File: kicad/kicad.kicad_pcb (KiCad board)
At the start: 2 copper layers, 106 parts, among them K0 !,,,,,,1, K1 ",,,,,,2, K10 *,,,,,,:, K11 =,,,,,,-, K12 Break, K13 Up, K14 Q, K15 W, K16 E, K17 R, K18 T, K19 Y, K2 #,,,,,,3, K20 U, K21 I, K22 O, K23 P, K24 @, K25 Left, K26 Right, K27 Down, K28 A, K29 S, K3 $,,,,,,4, K30 D, K31 F, K32 G, K33 H, K34 J, K35 K, K36 L, K37 +,,,,,,;, K38 ENTER, K39 CLEAR, K4 %,,,,,,5, K40 SHIFT, K41 Z, K42 X, K43 C, K44 V, K45 B, K46 N, K47 M, K48 <,,,,,,,, K49 >,,,,,,., K5 &,,,,,,6, K50 ?,,,,,,/, K51 SHIFT, K52 Blank, K6 ',,,,,,7, K7 (,,,,,,8, K8 ),,,,,,9, K9 0

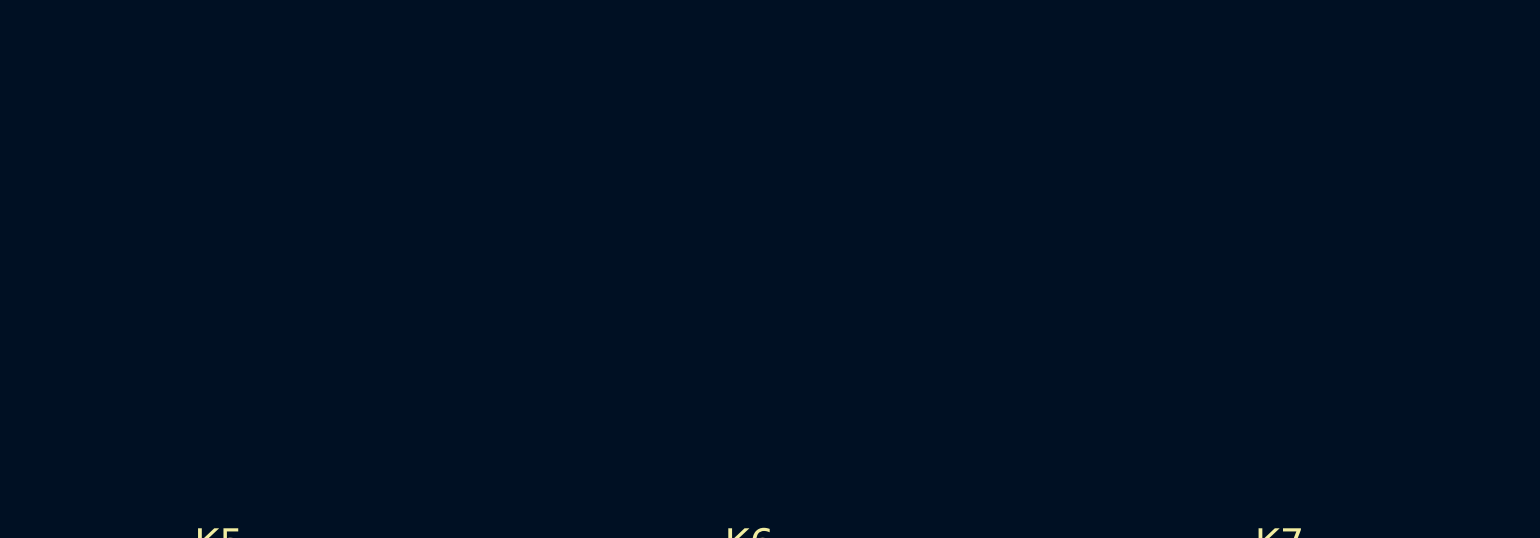
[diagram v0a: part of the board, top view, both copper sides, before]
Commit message: Matrix laid out
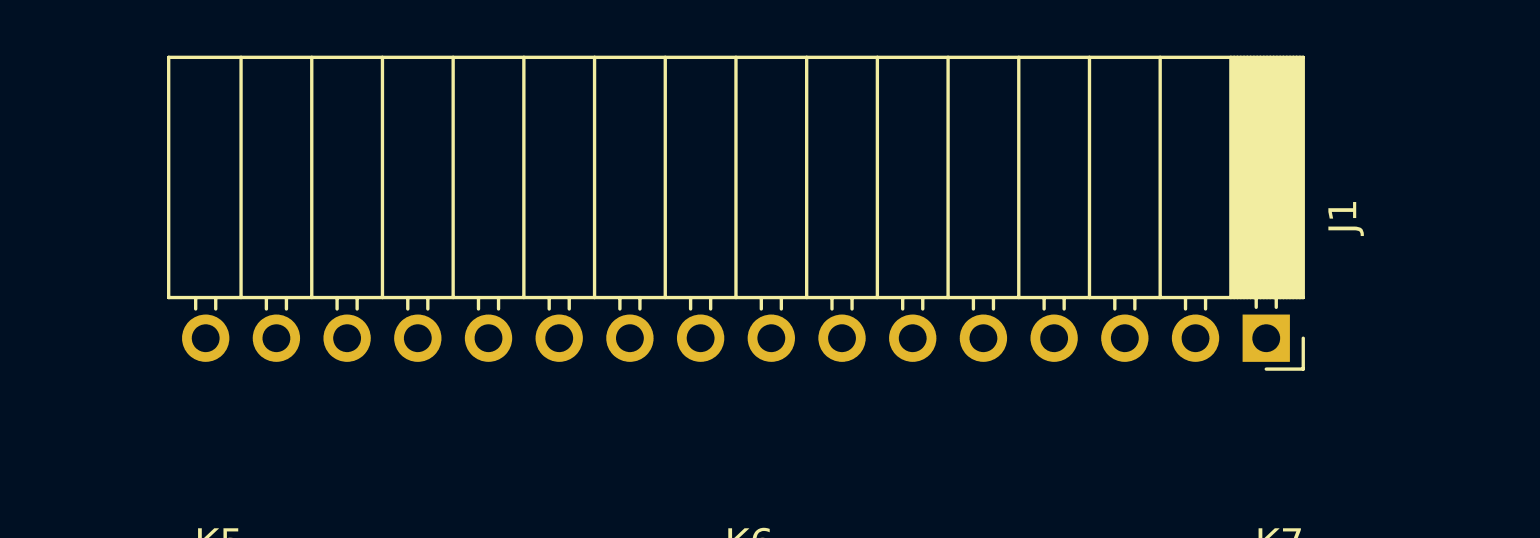
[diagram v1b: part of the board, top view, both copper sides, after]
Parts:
- added J1: Conn_01x16_Pin, Connector_PinSocket_2.54mm:PinSocket_1x16_P2.54mm_Horizontal, F.Cu at (234.9, 98.4)
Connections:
- D0 pad 1: /Row_0 -> /Row5
- D1 pad 1: /Row_0 -> /Row5
- D10 pad 1: /Row_0 -> /Row6
- D11 pad 1: /Row_0 -> /Row6
- D12 pad 1: /Row_0 -> /Row7
- D13 pad 1: /Row_1 -> /Row4
- D14 pad 1: /Row_1 -> /Row3
- D15 pad 1: /Row_1 -> /Row3
- D16 pad 1: /Row_1 -> /Row1
- D17 pad 1: /Row_1 -> /Row3
- D18 pad 1: /Row_1 -> /Row3
- D19 pad 1: /Row_1 -> /Row4
- D2 pad 1: /Row_0 -> /Row5
- D20 pad 1: /Row_1 -> /Row3
- D21 pad 1: /Row_1 -> /Row2
- D22 pad 1: /Row_1 -> /Row2
- D23 pad 1: /Row_1 -> /Row3
- D24 pad 1: /Row_1 -> /Row1
- D25 pad 1: /Row_1 -> /Row4
- D26 pad 1: /Row_1 -> /Row4
- D27 pad 1: /Row_2 -> /Row4
- D28 pad 1: /Row_2 -> /Row1
- D29 pad 1: /Row_2 -> /Row3
- D3 pad 1: /Row_0 -> /Row5
- D30 pad 1: /Row_2 -> /Row1
- D31 pad 1: /Row_2 -> /Row1
- D32 pad 1: /Row_2 -> /Row1
- D33 pad 1: /Row_2 -> /Row2
- D34 pad 1: /Row_2 -> /Row2
- D35 pad 1: /Row_2 -> /Row2
- D36 pad 1: /Row_2 -> /Row2
- D37 pad 1: /Row_2 -> /Row6
- D38 pad 1: /Row_2 -> /Row7
- D39 pad 1: /Row_2 -> /Row7
- D4 pad 1: /Row_0 -> /Row5
- D5 pad 1: /Row_0 -> /Row5
- D6 pad 1: /Row_0 -> /Row5
- D7 pad 1: /Row_0 -> /Row6
- D8 pad 1: /Row_0 -> /Row6
- D9 pad 1: /Row_0 -> /Row5
- K0 pad 1: /Col_0 -> /Col2
- K1 pad 1: /Col_1 -> /Col3
- K10 pad 1: /Col_10 -> /Col2
- K11 pad 1: /Col_11 -> /Col6
- K12 pad 1: /Col_12 -> /Col3
- K13 pad 1: /Col_0 -> /Col4
- K14 pad 1: /Col_1 -> /Col2
- K15 pad 1: /Col_2 -> /Col8
- K16 pad 1: /Col_3 -> /Col6
- K17 pad 1: /Col_4 -> /Col3
- K18 pad 1: /Col_5 -> /Col5
- K19 pad 1: /Col_6 -> /Col2
- K2 pad 1: /Col_2 -> /Col4
- K20 pad 1: /Col_7 -> /Col6
- K21 pad 1: /Col_8 -> /Col2
- K22 pad 1: /Col_9 -> /Col8
- K23 pad 1: /Col_10 -> /Col1
- K24 pad 1: /Col_11 -> /Col1
- K25 pad 1: /Col_12 -> /Col6
- K26 pad 1: /Col_13 -> /Col7
- K27 pad 1: /Col_0 -> /Col5
- K28 pad 1: /Col_1 -> /Col2
- K29 pad 1: /Col_2 -> /Col4
- K3 pad 1: /Col_3 -> /Col5
- K30 pad 1: /Col_3 -> /Col5
- K31 pad 1: /Col_4 -> /Col7
- K32 pad 1: /Col_5 -> /Col8
- K33 pad 1: /Col_6 -> /Col1
- K34 pad 1: /Col_7 -> /Col3
- K35 pad 1: /Col_8 -> /Col4
- K36 pad 1: /Col_9 -> /Col5
- K37 pad 1: /Col_10 -> /Col4
- K38 pad 1: /Col_11 -> /Col1
- K39 pad 1: /Col_12 -> /Col2
- K4 pad 1: /Col_4 -> /Col6
- K5 pad 1: /Col_5 -> /Col7
- K6 pad 1: /Col_6 -> /Col8
- K7 pad 1: /Col_7 -> /Col1
- K8 pad 1: /Col_8 -> /Col2
- K9 pad 1: /Col_9 -> /Col1

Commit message: Diodes removed, mounts added
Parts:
- removed D0, D1, D10, D11, D12, D13, D14, D15, D16, D17, D18, D19, D2, D20, D21, D22, D23, D24, D25, D26, D27, D28, D29, D3, D30, D31, D32, D33, D34, D35, D36, D37, D38, D39, D4, D40, D41, D42, D43, D44, D45, D46, D47, D48, D49, D5, D50, D51, D52, D6, D7, D8, D9: D, Diode_SMD:D_0805_2012Metric_Pad1.15x1.40mm_HandSolder
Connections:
- K0 pad 2: Net-(D0-A) -> /Row5
- K1 pad 2: Net-(D1-A) -> /Row5
- K10 pad 2: Net-(D10-A) -> /Row6
- K11 pad 2: Net-(D11-A) -> /Row6
- K12 pad 2: Net-(D12-A) -> /Row7
- K13 pad 2: Net-(D13-A) -> /Row4
- K14 pad 2: Net-(D14-A) -> /Row3
- K15 pad 2: Net-(D15-A) -> /Row3
- K16 pad 2: Net-(D16-A) -> /Row1
- K17 pad 2: Net-(D17-A) -> /Row3
- K18 pad 2: Net-(D18-A) -> /Row3
- K19 pad 2: Net-(D19-A) -> /Row4
- K2 pad 2: Net-(D2-A) -> /Row5
- K20 pad 2: Net-(D20-A) -> /Row3
- K21 pad 2: Net-(D21-A) -> /Row2
- K22 pad 2: Net-(D22-A) -> /Row2
- K23 pad 2: Net-(D23-A) -> /Row3
- K24 pad 2: Net-(D24-A) -> /Row1
- K25 pad 2: Net-(D25-A) -> /Row4
- K26 pad 2: Net-(D26-A) -> /Row4
- K27 pad 2: Net-(D27-A) -> /Row4
- K28 pad 2: Net-(D28-A) -> /Row1
- K29 pad 2: Net-(D29-A) -> /Row3
- K3 pad 2: Net-(D3-A) -> /Row5
- K30 pad 2: Net-(D30-A) -> /Row1
- K31 pad 2: Net-(D31-A) -> /Row1
- K32 pad 2: Net-(D32-A) -> /Row1
- K33 pad 2: Net-(D33-A) -> /Row2
- K34 pad 2: Net-(D34-A) -> /Row2
- K35 pad 2: Net-(D35-A) -> /Row2
- K36 pad 2: Net-(D36-A) -> /Row2
- K37 pad 2: Net-(D37-A) -> /Row6
- K38 pad 2: Net-(D38-A) -> /Row7
- K39 pad 2: Net-(D39-A) -> /Row7
- K4 pad 2: Net-(D4-A) -> /Row5
- K40 pad 2: Net-(D40-A) -> /Row7
- K41 pad 2: Net-(D41-A) -> /Row4
- K42 pad 2: Net-(D42-A) -> /Row4
- K43 pad 2: Net-(D43-A) -> /Row1
- K44 pad 2: Net-(D44-A) -> /Row3
- K45 pad 2: Net-(D45-A) -> /Row1
- K46 pad 2: Net-(D46-A) -> /Row2
- K47 pad 2: Net-(D47-A) -> /Row2
- K48 pad 2: Net-(D48-A) -> /Row6
- K49 pad 2: Net-(D49-A) -> /Row6
- K5 pad 2: Net-(D5-A) -> /Row5
- K50 pad 2: Net-(D50-A) -> /Row6
- K51 pad 2: Net-(D51-A) -> /Row7
- K52 pad 2: Net-(D52-A) -> /Row5
- K6 pad 2: Net-(D6-A) -> /Row5
- K7 pad 2: Net-(D7-A) -> /Row6
- K8 pad 2: Net-(D8-A) -> /Row6
- K9 pad 2: Net-(D9-A) -> /Row5

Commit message: Routed
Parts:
- removed J1: Conn_01x16_Pin, Connector_PinSocket_2.54mm:PinSocket_1x16_P2.54mm_Horizontal
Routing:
- net /Col8: track 0.00 -> 431.5 mm, vias 0 -> 6
- net /Col3: track 0.00 -> 392.7 mm, vias 0 -> 6
- net /Col2: track 0.00 -> 351.3 mm, vias 0 -> 5
- net /Row7: track 0.00 -> 328.6 mm, vias 0 -> 1
- net /Row4: track 0.00 -> 323.1 mm, vias 0 -> 4
- net /Col1: track 0.00 -> 297.6 mm, vias 0 -> 4
- net /Row1: track 0.00 -> 294.0 mm, vias 0 -> 4
- net /Col7: track 0.00 -> 285.1 mm, vias 0 -> 4
- net /Col6: track 0.00 -> 281.2 mm, vias 0 -> 5
- net /Col4: track 0.00 -> 279.0 mm, vias 0 -> 4
- net /Col5: track 0.00 -> 266.0 mm, vias 0 -> 3
- net /Row5: track 0.00 -> 252.3 mm
- net /Row3: track 0.00 -> 239.0 mm
- net /Row6: track 0.00 -> 187.0 mm, vias 0 -> 1
- net /Row2: track 0.00 -> 142.2 mm

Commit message: Terrible board outline
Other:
- board outline added: 315 x 123 mm

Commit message: Aligned
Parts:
- moved K40 225.4 mm to (68.6, -57.8)
- moved K41 225.4 mm to (99.6, -57.8)
- moved K42 225.4 mm to (118.6, -57.8)
- moved K43 225.4 mm to (137.7, -57.8)
- moved K44 225.4 mm to (156.7, -57.8)
- moved K45 225.4 mm to (175.8, -57.8)
- moved K46 225.4 mm to (194.8, -57.8)
- moved K47 225.4 mm to (213.9, -57.8)
- moved K48 225.4 mm to (232.9, -57.8)
- moved K49 225.4 mm to (252.0, -57.8)
- moved K50 225.4 mm to (271.0, -57.8)
- moved K51 225.4 mm to (302.0, -57.8)
- moved K0 225.4 mm to (75.7, -115.0)
- moved K1 225.4 mm to (94.8, -115.0)
- moved K10 225.4 mm to (266.2, -115.0)
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
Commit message: Nice diagram
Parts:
- moved K40 211.3 mm to (109.6, 149.5)
- moved K41 211.3 mm to (140.6, 149.5)
- moved K42 211.3 mm to (159.6, 149.5)
- moved K43 211.3 mm to (178.7, 149.5)
- moved K44 211.3 mm to (197.7, 149.5)
- moved K45 211.3 mm to (216.8, 149.5)
- moved K46 211.3 mm to (235.8, 149.5)
- moved K47 211.3 mm to (254.9, 149.5)
- moved K48 211.3 mm to (273.9, 149.5)
- moved K49 211.3 mm to (293.0, 149.5)
- moved K50 211.3 mm to (312.0, 149.5)
- moved K51 211.3 mm to (343.0, 149.5)
- moved K0 211.3 mm to (116.8, 92.3)
- moved K1 211.3 mm to (135.8, 92.3)
- moved K10 211.3 mm to (307.3, 92.3)
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
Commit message: Critical dimension checked, we're good to go
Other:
- board text added: "coco keyboard insert v1 leadedsolder.com 2024"
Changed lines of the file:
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@@
 			(sketchpadsonfab no)
 			(subtractmaskfromsilk no)
-			(outputformat 1)
+			(outputformat 4)
 			(mirror no)
-			(drillshape 1)
+			(drillshape 0)
 			(scaleselection 1)
 			(outputdirectory "")
@@
 		(layer "Edge.Cuts")
 	)
+	(gr_text "coco keyboard insert v1\nleadedsolder.com 2024"
+		(at 353.175 189.675 0)
+		(layer "F.SilkS")
+		(effects
+			(font
+				(size 1 1)
+				(thickness 0.15)
+			)
+			(justify left bottom)
+		)
+	)
 	(dimension

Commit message: Routed in the connector, although I need to double check
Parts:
- added J1: Conn_01x16_Pin, Connector_PinSocket_2.54mm:PinSocket_1x16_P2.54mm_Horizontal, F.Cu at (247.6, 88.0)
- moved K27 4.28 mm to (112.0, 134.7)
- moved K28 4.28 mm to (131.1, 134.7)
- moved K29 4.28 mm to (150.1, 134.7)
- moved K30 4.28 mm to (169.2, 134.7)
- moved K31 4.28 mm to (188.2, 134.7)
- moved K32 4.28 mm to (207.3, 134.7)
- moved K33 4.28 mm to (226.3, 134.7)
- moved K34 4.28 mm to (245.4, 134.7)
- moved K35 4.28 mm to (264.4, 134.7)
- moved K36 4.28 mm to (283.5, 134.7)
- moved K37 4.28 mm to (302.5, 134.7)
- moved K38 4.28 mm to (333.5, 134.7)
- moved K39 4.28 mm to (364.4, 134.7)
- moved K52 4.28 mm to (228.7, 172.8)
- moved K0 4.28 mm to (116.8, 96.6)
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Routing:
- net /Row7: track 328.6 -> 450.3 mm, vias 1 -> 2
- net /Row2: track 142.2 -> 203.8 mm, vias 0 -> 1
- net /Col4: track 279.0 -> 326.9 mm, vias 4 -> 5
- net /Col7: track 285.1 -> 330.3 mm, vias 4 -> 5
- net /Row1: track 294.0 -> 337.6 mm
- net /Col3: track 392.7 -> 432.1 mm, vias 6 -> 7
- net /Col8: track 431.5 -> 467.9 mm, vias 6 -> 7
- net /Row3: track 239.0 -> 268.8 mm, vias 0 -> 1
- net /Col2: track 351.3 -> 380.2 mm, vias 5 -> 6
- net /Row6: track 187.0 -> 215.6 mm, vias 1 -> 2
- net /Col1: track 297.6 -> 325.8 mm, vias 4 -> 5
- net /Row4: track 323.1 -> 349.0 mm
- net /Col5: track 266.0 -> 291.5 mm, vias 3 -> 4
- net /Col6: track 281.2 -> 300.4 mm
- net /Row5: track 252.3 -> 264.5 mm
